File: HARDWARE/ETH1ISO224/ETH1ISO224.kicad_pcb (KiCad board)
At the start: 2 copper layers, 100 x 45 mm, 145 parts, among them J201 1710072, J301 1715721, J401 20021111-00010T4LF, J501 RJ45_Wuerth_7499010121A, Q301 SI5618A, Q302 MMBT3904, U201 ISO224, U202 TBA1-0513E, U203 DG419LEDY, U204 DG412LEDQ, U205 OPA2340UA, U206 REF1925AIDDCT, U301 TSR_1-2450, U302 LM1117MP-3.3/NOPB, U401 LT6350xMS8, U402 REF1933AIDDCT, U403 STM32H743VITx, U404 24LC08B-E/MS, U501 LAN8742A, Y401 NX5032GA-16, Y501 NX5032GA-25

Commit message: Hardware design
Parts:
- added L201: 74438335100, Inductor_SMD:L_Wuerth_MAPI-3015, B.Cu at (109.2, 78.7)
- C201, F301, FID102, FID104: moved to B.Cu
- moved Y501 195.5 mm to (169.9, 74.8), turned to 180 degrees
- moved RN501 188.8 mm to (165.5, 80.9)
- moved FID104 166.2 mm to (190.1, 68.5), turned to 180 degrees
- moved U402 165.4 mm to (161.0, 73.7), turned to -90 degrees
- moved FID103 164.9 mm to (190.1, 68.5)
- moved U206 163.3 mm to (140.1, 101.0)
- moved U401 150.2 mm to (155.4, 73.7)
- moved U204 145.1 mm to (140.2, 85.7), turned to 90 degrees
- moved F301 135.9 mm to (191.1, 100.3), turned to -90 degrees
- moved C201 126.7 mm to (110.9, 75.2), turned to 180 degrees
- moved U302 121.7 mm to (171.8, 96.0), turned to 90 degrees
- moved FID101 79.5 mm to (110.2, 108.0)
- moved FID102 79.3 mm to (110.2, 108.0), turned to 180 degrees
- moved U205 7.07 mm to (140.2, 93.9)
- moved U201 4.81 mm to (129.7, 92.2)
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- renumbered R205 to R204, R206 to R205, R204 to R206, R222 to R220, R226 to R221, R223 to R222, R221 to R223, R225 to R224, R224 to R225, R220 to R226, RN202 to RN201, RN203 to RN202, RN204 to RN203, RN201 to RN204
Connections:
- R201 pad 2: Net-(J201-Pin_1) -> Net-(RN204-common)
- RN204 pad 1: Net-(J201-Pin_1) -> Net-(RN204-common)

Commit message: Hardware design
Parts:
- added C219: 0.1u, Capacitor_SMD:C_0603_1608Metric_Pad1.08x0.95mm_HandSolder, B.Cu at (137.7, 90.6)
- added C220: 0.1u, Capacitor_SMD:C_0603_1608Metric_Pad1.08x0.95mm_HandSolder, B.Cu at (141.4, 83.9)
- added C221: 0.1u, Capacitor_SMD:C_0603_1608Metric_Pad1.08x0.95mm_HandSolder, F.Cu at (138.6, 68.3)
- added C222: 0.1u, Capacitor_SMD:C_0603_1608Metric_Pad1.08x0.95mm_HandSolder, F.Cu at (142.0, 68.3)
- added C223: 0.1u, Capacitor_SMD:C_0603_1608Metric_Pad1.08x0.95mm_HandSolder, B.Cu at (141.4, 79.0)
- C201: moved to F.Cu
- C202, C203, C204, C206, C207, C208, C209, C210, C211, C214, C215, C217, C301, C302, C304, C401, C402, C403, C404, C405, C406, C408, C409, C410, C412, C414, C415, C416, C417, C418, C419, C420, C501, C502, C504, C505, C506, C509, C510, C511, C512, D301, D302, FB401, R205, R210, R211, R212, R213, R214, R216, R217, R218, R302, R402, R406, R407, R408, R502, R503, R504, R505, R506, RN502, RN503, U404, Y401: moved to B.Cu
- R219: value 100k/0.05% -> 51k/.05%
- R223: value 100k/.05% -> 51k/.05%
- R225: value 3k/.05% -> 511/.05%
- R226: value 0 -> 511/.05%
- moved C512 218.7 mm to (183.0, 74.7), turned to 90 degrees
- moved C504 211.6 mm to (171.7, 73.8), turned to 90 degrees
- moved C511 210.6 mm to (180.5, 88.5), turned to -90 degrees
- moved R506 208.7 mm to (177.5, 74.7), turned to 90 degrees
- moved C505 208.1 mm to (168.5, 77.9), turned to 90 degrees
- moved C507 207.1 mm to (169.0, 86.9), turned to 180 degrees
- moved C502 206.8 mm to (170.1, 77.9), turned to 90 degrees
- moved C506 206.2 mm to (165.1, 77.2), turned to 180 degrees
- moved C501 205.1 mm to (167.6, 73.8), turned to 90 degrees
- moved C510 204.6 mm to (173.4, 83.8), turned to -90 degrees
- moved C509 204.4 mm to (171.8, 77.9), turned to 90 degrees
- moved R505 204.1 mm to (177.5, 85.0), turned to -90 degrees
- moved C503 203.3 mm to (165.1, 77.2), turned to 180 degrees
- moved R504 201.8 mm to (173.5, 77.9), turned to -90 degrees
- moved R503 201.4 mm to (177.5, 88.5), turned to -90 degrees
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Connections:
- C206 pad 1: +5V -> +5VA
- C207 pad 1: +5V -> +5VA
- C208 pad 1: +5V -> +5VA
- C402 pad 1: +5V -> +5VA
- C405 pad 1: +5V -> +5VA
- U202 pad 1: +5V -> +5VA
- U402 pad 3: +5V -> +5VA
- U402 pad 4: +5V -> +5VA
- U403 pad 25: unconnected-(U403-PA3-Pad25) -> /Analog/MCU_G100
- U403 pad 28: /Analog/MCU_G100 -> /Analog/MCU_G10
- U403 pad 29: /Analog/MCU_G10 -> /Analog/MCU_G1
- U403 pad 30: unconnected-(U403-PA6-Pad30) -> /Analog/MCU_ZOFFS
- U403 pad 35: /Analog/MCU_ZOFFS -> unconnected-(U403-PB1-Pad35)
- U403 pad 36: /Analog/MCU_G1 -> unconnected-(U403-PB2-Pad36)
- U403 pad 64: /MCU/LED_RED -> unconnected-(U403-PC7-Pad64)
- U403 pad 66: unconnected-(U403-PC9-Pad66) -> /MCU/LED_RED
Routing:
- net GND1: track 0.00 -> 110.1 mm, vias 0 -> 2
- net +3.3V: track 0.00 -> 81.3 mm, vias 0 -> 18
- net +2V5: track 0.00 -> 62.0 mm, vias 0 -> 4
- net GND: track 0.00 -> 56.4 mm, vias 0 -> 13
- net /MCU/NRST: track 0.00 -> 48.7 mm, vias 0 -> 2
- net Net-(R216-Pad1): track 0.00 -> 44.1 mm, vias 0 -> 3
- net +1V25: track 0.00 -> 36.2 mm, vias 0 -> 2
- net VCCQ: track 0.00 -> 35.6 mm, vias 0 -> 6
- net /Ethernet/RMII_TXD1: track 0.00 -> 30.7 mm, vias 0 -> 2
- net /Ethernet/RMII_TXD0: track 0.00 -> 30.5 mm, vias 0 -> 2
- net Net-(C209-Pad2): track 0.00 -> 30.0 mm, vias 0 -> 2
- net /Ethernet/RMII_TXEN: track 0.00 -> 29.4 mm, vias 0 -> 2
- net Net-(U205B--): track 0.00 -> 28.3 mm
- net /Ethernet/RMII_MDIO: track 0.00 -> 26.7 mm, vias 0 -> 2
- net Net-(D301-A): track 0.00 -> 26.6 mm, vias 0 -> 1
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- added copper zone on B.Cu, net +3.3V
- added copper zone on F.Cu, net +3.3V
- added copper zone on In2.Cu, net +3.3V
- added copper zone on B.Cu, net +5V
- added copper zone on F.Cu, net +5V
- added copper zone on In2.Cu, net +5V
- added copper zone on B.Cu, net +5VA
- added copper zone on F.Cu, net +5VA
- added copper zone on In2.Cu, net +5VA
- added copper zone on B.Cu, net Earth
- added copper zone on F.Cu, net Earth
- added copper zone on B.Cu, net GND
- added copper zone on F.Cu, net GND
- added copper zone on In1.Cu, net GND
- added copper zone on B.Cu, net Net-(D301-K)
- added copper zone on F.Cu, net Net-(D301-K)
- added copper zone on B.Cu, net Net-(J301-Pin_1)
- added copper zone on B.Cu, net Net-(Q301-D)
- added copper zone on F.Cu, net Net-(Q301-D)
- added copper zone on B.Cu, net VCCQ
- added copper zone on F.Cu, net VCCQ
- added copper zone on In2.Cu, net VCCQ
- added copper zone on B.Cu, net VDDA
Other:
- copper layers 2 -> 4

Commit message: Hardware design
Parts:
- added SYM201: SYM_Flash_Small, ETH1ISO224:Symbol_Attention_Triangle_8x7mm_Copper, F.Cu at (108.3, 73.2)
- added SYM202: SYM_Flash_Small, ETH1ISO224:Symbol_Attention_Triangle_8x7mm_Copper, B.Cu at (109.1, 98.9)
- U202: value TBA1-0513E -> TBA 1-0511HI; footprint Converter_DCDC:Converter_DCDC_TRACO_TBA1-xxxxE_Single_THT -> ETH1ISO224:TBA1
- moved U202 7.77 mm to (126.2, 105.7), turned to 180 degrees
- moved C201 1.27 mm to (120.9, 72.8)
- moved R204 1.27 mm to (120.9, 68.8)
- moved C203 1.02 mm to (117.3, 103.9)
- moved C204 1.02 mm to (117.3, 105.5)
- moved C202 0.76 mm to (122.0, 104.8)
- moved FID101 0.76 mm to (109.5, 108.0)
- moved FID102 0.76 mm to (109.5, 108.0)
- moved FID103 0.38 mm to (190.5, 68.5)
- moved FID104 0.38 mm to (190.5, 68.5)
- moved J301 0.38 mm to (195.2, 98.9)
- moved RN204 0.38 mm to (116.7, 89.2)
- moved U301 0.25 mm to (185.6, 93.9)
- moved R205 0.13 mm to (123.8, 70.7)
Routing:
- net (no net): track 0.00 -> 84.3 mm
- net GND: track 56.4 -> 74.3 mm, vias 13 -> 28
- net GND1: track 110.1 -> 95.5 mm
- net /Ethernet/ETH_RXP: track 2.73 -> 16.0 mm
- net /Ethernet/ETH_RXN: track 3.43 -> 16.7 mm
- net /Ethernet/ETH_TXP: track 6.35 -> 18.3 mm, vias 0 -> 1
- net /Ethernet/ETH_TXN: track 5.46 -> 17.2 mm, vias 0 -> 1
- net /Ethernet/REF_CLK: track 18.8 -> 30.5 mm
- net /Ethernet/RMII_MDC: track 21.5 -> 30.8 mm
- net /Ethernet/RMII_CRS_DV: track 21.5 -> 30.5 mm
- net /MCU/NRST: track 48.7 -> 57.7 mm
- net /Ethernet/RMII_RXD1: track 22.3 -> 30.5 mm
- net /Ethernet/RMII_RXD0: track 22.3 -> 30.5 mm
- net /Ethernet/RMII_MDIO: track 26.7 -> 34.4 mm
- net +5V: track 2.69 -> 1.14 mm
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- added copper zone on B.Cu, net +15V
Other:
- board text added: "+24 VDC"
- board text added: "1"
- board text added: "2"
- board text added: "3"
- board text added: "4"
- board text added: "ETH1ISO224 V1.0 Default IP : 192.168.1.21"
- board text added: "VOLTAGE MEASUREMENT"

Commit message: Hardware design
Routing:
- net GND: track 74.3 -> 76.7 mm, vias 28 -> 30

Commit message: Hardware design
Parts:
- removed the C213 at (138.7, 106.4)
- removed the C214 at (138.7, 106.4)
- removed the C215 at (141.0, 106.4)
- removed the C216 at (141.0, 106.4)
- removed the C217 at (142.7, 101.7)
- removed the C218 at (142.7, 101.7)
- removed the R219 at (156.0, 69.2)
- removed R222: 0, Resistor_SMD:R_0603_1608Metric_Pad0.98x0.95mm_HandSolder
- removed R223: 51k/.05%, Resistor_SMD:R_0603_1608Metric_Pad0.98x0.95mm_HandSolder
- removed R224: 100k/.05%, Resistor_SMD:R_0603_1608Metric_Pad0.98x0.95mm_HandSolder
- removed R225, R226: 511/.05%, Resistor_SMD:R_0603_1608Metric_Pad0.98x0.95mm_HandSolder
- removed the RN203 at (159.9, 69.1)
- removed the U202 at (126.2, 105.7)
- added C211: 0.1u, Capacitor_SMD:C_0603_1608Metric_Pad1.08x0.95mm_HandSolder, B.Cu at (148.6, 69.6)
- added C409: 0.1u, Capacitor_SMD:C_0603_1608Metric_Pad1.08x0.95mm_HandSolder, B.Cu at (158.8, 76.5)
- added C411: 1u, Capacitor_SMD:C_0603_1608Metric_Pad1.08x0.95mm_HandSolder, B.Cu at (160.3, 76.5)
- added D201: 1N4148W, Diode_SMD:D_SOD-123, F.Cu at (152.4, 68.8)
- added U203: TBA 1-0511HI, ETH1ISO224:TBA 1HI, F.Cu at (126.2, 105.7)
- R210: renamed from R221; value 100k -> 10k
- R213: renamed from R212; value 10k/.05% -> 5k/.05%
- R214: renamed from R213; value 10k/.05% -> 5k/.05%
- R216: renamed from R215; value 100k/0.1% -> 100k/0.05%
- R220: value 100k/0.05% -> 0
- RN202: renamed from RN201; value MPMT2003AT5 -> MPMT50011002AT5
- RN203: renamed from RN202; value MPMT2003AT5 -> MPMT50011002AT5
- U206: value REF1925AIDDCT -> LT6015IS5; footprint Package_TO_SOT_SMD:SOT-23-5_HandSoldering -> Package_TO_SOT_SMD:SOT-23-5
- moved U206 33.6 mm to (147.7, 69.6), turned to 0 degrees
- moved FB201 10.7 mm to (141.2, 107.1)
- moved C217 8.35 mm to (139.3, 102.9), turned to 90 degrees
- moved C218 8.35 mm to (139.3, 102.9), turned to 90 degrees
- moved C412 3.44 mm to (161.5, 83.6), turned to -90 degrees
- moved R220 3.00 mm to (153.0, 70.9)
- moved D401 2.57 mm to (156.1, 106.9)
- moved R211 1.78 mm to (142.7, 96.5)
- moved R213 1.52 mm to (141.2, 96.5)
- moved R406 0.76 mm to (161.5, 87.2)
- moved RN201 0.70 mm to (116.7, 89.9)
- moved C209 0.25 mm to (136.0, 96.5)
- moved R214 0.25 mm to (137.5, 96.5)
- moved C203 0.13 mm to (117.3, 104.0)
- renumbered C221 to C212, C219 to C213, C220 to C214, C222 to C215, C223 to C216, C211 to C217, C212 to C218, C409 to C410, C410 to C412, C411 to C413, C412 to C414, C413 to C415, C414 to C416, C415 to C417, C416 to C418, C417 to C419, C418 to C420, C419 to C421, C420 to C422, R210 to R211, R211 to R212, R214 to R215, R216 to R217, R217 to R218, R218 to R219, RN204 to RN201, U204 to U201, U201 to U202, U203 to U204
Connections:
- C210 pad 2: +2V5 -> VCOM
- R211 pad 1: Net-(U201-OUT+) -> Net-(U202-OUT+)
- R212 pad 1: Net-(U201-OUT-) -> Net-(U202-OUT-)
- R213 pad 1: +2V5 -> VCOM
- R215 pad 2: +2V5 -> VCOM
- R216 pad 2: +2V5 -> VCOM
- R217 pad 1: Net-(R216-Pad1) -> Net-(D201-A)
- R219 pad 2: +2V5 -> VCOM
- R220 pad 1: GND -> Net-(D201-A)
- RN202 pad 1: Net-(U201-OUT+) -> VCOM
- RN202 pad 2: +2V5 -> Net-(U202-OUT+)
- RN203 pad 1: Net-(U201-OUT-) -> Net-(C209-Pad2)
- RN203 pad 2: Net-(C209-Pad2) -> Net-(U202-OUT-)
- U201 pad 3: Net-(R216-Pad1) -> Net-(D201-A)
- U202 pad 6: Net-(U201-OUT-) -> Net-(U202-OUT-)
- U202 pad 7: Net-(U201-OUT+) -> Net-(U202-OUT+)
- U205 pad 7: Net-(R216-Pad1) -> Net-(D201-A)
- U206 pad 1: +1V25 -> Net-(D201-K)
- U206 pad 3: +5VA -> +3.3V
- U206 pad 4: +5VA -> Net-(D201-A)
- U206 pad 5: +2V5 -> +5VA
- U402 pad 1: unconnected-(U402-Vbias-Pad1) -> VCOM
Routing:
- net +2V5: track 62.4 -> 0.00 mm, vias 4 -> 0
- net VCOM: track 13.1 -> 72.9 mm, vias 0 -> 4
- net Net-(R216-Pad1): track 44.2 -> 0.00 mm, vias 3 -> 0
- net Net-(D201-A): track 0.00 -> 36.4 mm, vias 0 -> 3
- net +1V25: track 35.6 -> 0.00 mm, vias 2 -> 0
- net Net-(U202-OUT+): track 0.00 -> 15.4 mm, vias 0 -> 1
- net Net-(U201-OUT+): track 12.5 -> 0.00 mm, vias 1 -> 0
- net Net-(U202-OUT-): track 0.00 -> 8.25 mm, vias 0 -> 1
- net Net-(U201-OUT-): track 7.27 -> 0.00 mm, vias 1 -> 0
- net +3.3V: track 81.9 -> 88.2 mm
- net /Analog/VOUT: track 17.6 -> 12.1 mm
- net Net-(D201-K): track 0.00 -> 4.95 mm
- net Net-(U205A-+): track 11.2 -> 6.41 mm
- net +5VA: track 20.5 -> 16.4 mm
- net Net-(C209-Pad2): track 30.3 -> 26.9 mm
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
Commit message: Hardware design done
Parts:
- removed the R201 at (118.2, 74.7)
- added C211: 0.1u, Capacitor_SMD:C_0603_1608Metric_Pad1.08x0.95mm_HandSolder, B.Cu at (160.3, 69.1)
- added R214: 0, Resistor_SMD:R_0603_1608Metric_Pad0.98x0.95mm_HandSolder, F.Cu at (158.0, 69.6)
- added R221: 1k, Resistor_SMD:R_0603_1608Metric_Pad0.98x0.95mm_HandSolder, B.Cu at (152.9, 69.6)
- added U208: MCP6001-OT, Package_TO_SOT_SMD:SOT-23-5, F.Cu at (160.9, 69.6)
- C201: value 10n/2k -> 0.01u/1.5k
- L201: value 74438335100 -> 74438336100
- U202: renamed from U203; value TBA 1-0511HI -> TBA 1-0513HI
- U401: value LT6350xMS8 -> LT6350IMS8
- moved R215 1.66 mm to (137.7, 85.9)
- moved D201 0.89 mm to (151.5, 68.8)
- moved R219 0.89 mm to (152.1, 70.9)
- moved U207 0.89 mm to (146.8, 69.6)
- moved R201 0.80 mm to (122.0, 77.6)
- moved C212 0.51 mm to (149.1, 69.6)
- moved SYM202 0.40 mm to (109.2, 98.6)
- moved R202 0.25 mm to (120.1, 82.5)
- moved R203 0.25 mm to (120.1, 87.5)
- moved SYM201 0.25 mm to (108.1, 73.2)
- moved C203 0.13 mm to (117.3, 104.1)
- moved C204 0.13 mm to (117.3, 105.7)
- renumbered C211 to C212, C212 to C213, C213 to C214, C214 to C215, C215 to C216, C216 to C217, C217 to C218, C218 to C219, R202 to R201, R203 to R202, R206 to R203, R207 to R206, R208 to R207, R209 to R208, R211 to R209, R212 to R210, R213 to R211, R214 to R212, R215 to R213, R216 to R215, R217 to R216, R218 to R217, R219 to R218, R220 to R219, R210 to R220, U202 to U201, U204 to U203, U201 to U204, U206 to U207
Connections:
- R201 pad 2: Net-(R201-Pad1) (its old number) -> Net-(RN201-common)
- R215 pad 2: VCOM -> Net-(U208--)
- R216 pad 1: Net-(D201-A) -> Net-(R216-Pad1)
- R218 pad 2: VCOM -> Net-(U208--)
- U204 pad 3: Net-(D201-A) -> Net-(R216-Pad1)
- U205 pad 7: Net-(D201-A) -> Net-(R216-Pad1)
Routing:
- net Net-(U208--): track 0.00 -> 67.5 mm, vias 0 -> 1
- net Net-(R216-Pad1): track 0.00 -> 33.3 mm, vias 0 -> 2
- net Net-(D201-A): track 36.4 -> 7.58 mm, vias 3 -> 1
- net VCOM: track 72.9 -> 83.0 mm
- net GND: track 74.1 -> 81.8 mm, vias 31 -> 36
- net GND1: track 94.3 -> 98.3 mm
- net Net-(R201-Pad1) (its old number): track 3.78 -> 0.00 mm
- net /Analog/MCU_G1: track 18.0 -> 15.9 mm
- net Net-(D301-K): track 2.14 -> 0.00 mm
- net +5VA: track 16.4 -> 17.8 mm, vias 9 -> 10
- net Net-(RN201-common): track 12.3 -> 13.5 mm
- net Net-(U205B-+): track 6.66 -> 7.54 mm
- net Net-(D201-K): track 4.95 -> 5.74 mm
- net Net-(C209-Pad2): track 26.9 -> 26.2 mm
- net +3.3V: track 88.2 -> 87.5 mm
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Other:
- board text added: "ETH1ISO224 V1.1 Default IP : 192.168.1.21"
- board text removed: "ETH1ISO224 V1.0 Default IP : 192.168.1.21"

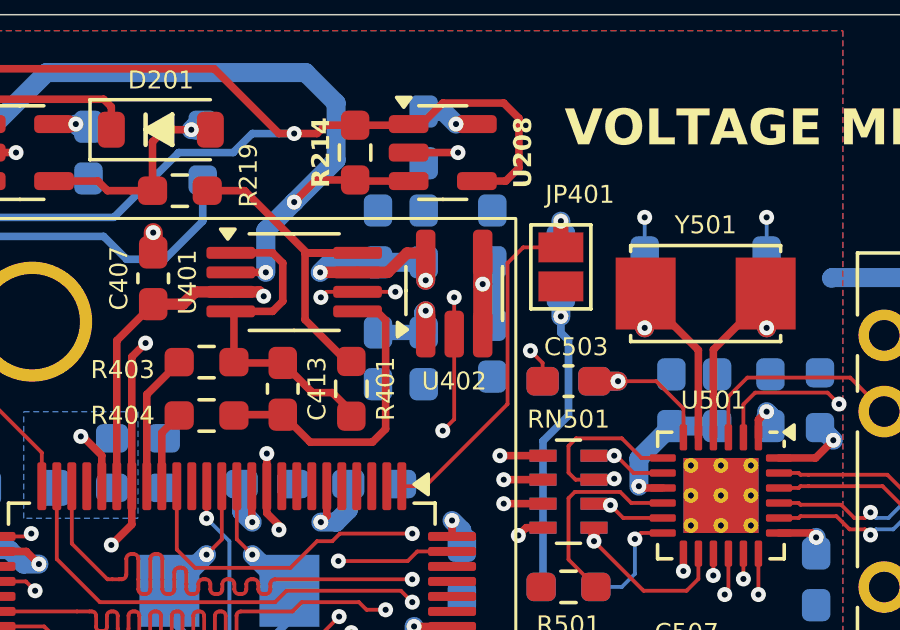
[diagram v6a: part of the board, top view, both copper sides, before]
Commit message: Footprint change, not critical
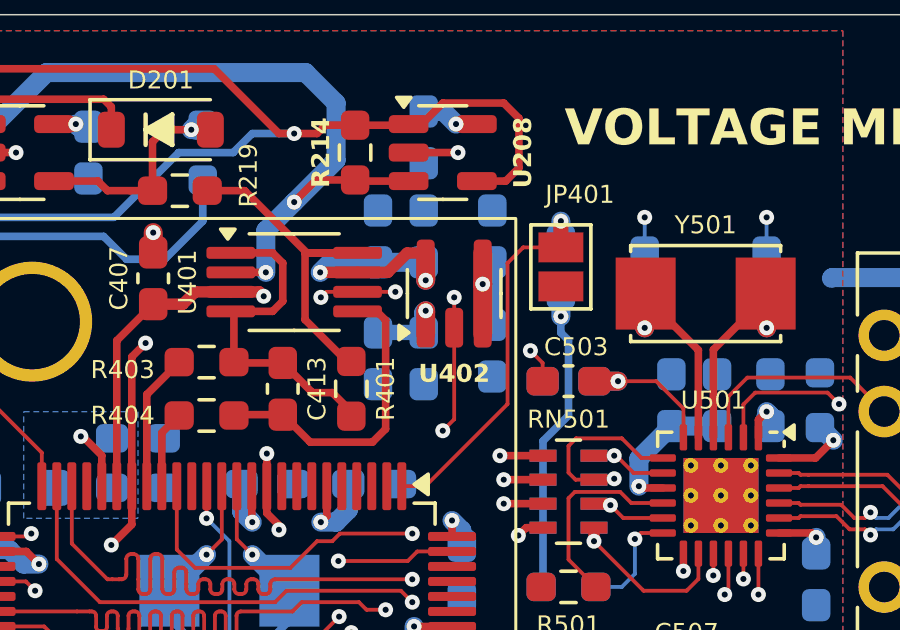
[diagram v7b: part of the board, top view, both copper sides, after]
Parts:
- U402: footprint Package_TO_SOT_SMD:SOT-23-5_HandSoldering -> Package_TO_SOT_SMD:SOT-23-5

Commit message: Hardware changes
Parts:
- moved C302 0.64 mm to (190.6, 92.6)
- moved J301 0.60 mm to (195.3, 98.3)
- moved C301 0.56 mm to (190.6, 95.0)
- moved J501 0.19 mm to (180.3, 76.6)
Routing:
- net /Ethernet/ETH_TXP: track 18.3 -> 17.7 mm
